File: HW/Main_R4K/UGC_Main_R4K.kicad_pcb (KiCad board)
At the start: 4 copper layers, 125.7 x 76.4 mm, 167 parts, among them J1 SM02B-SURS-TF_LF__SN_, J10 SM02B-SURS-TF_LF__SN_, J13 503480-0640, J2 503480-0640, J4 Conn_01x06_Pin, J5 UJ31-CH-G1-SMT-TR, J6 Trigger, J7 Trigger, J8 Conn_01x02, J9 Conn_01x02, Q1 MMBT3904, Q2 MMBT3904, Q3 BSS138DW, Q4 BSS138DW, Q5 MMBT2222A, Q6 MMBT2222A, SW1 SW_Push, SW10 SW_Push, SW11 SW_Push, SW12 SW_Push, SW13 SW_Push, SW14 SW_TS-1187A, SW15 1TS026A-1000-0550, SW16 1TS026A-1000-0550, SW17 SW_TS-1187A, SW18 SW_TS-1187A, SW19 SW_TS-1187A, SW2 SW_Push, SW3 SW_Push, SW4 SW_Push, SW5 SW_TS-1187A, SW6 GL18_SW, SW7 SW_Push, SW8 SW_Push, SW9 SW_TS-1187A, U1 ESP32-PICO-MINI-02, U10 ST_LSM6, U11 BQ25180, U12 CH340K, U13 PI3USB4000A, U4 TPS630001RCR, U5 ST_LSM6, U6 MCP3002, U7 MCP3002, U8 RP2040, U9 GD25Q80EEIGR, X1 ModConnect, X2 ModConnect, X3 ModConnect, X4 ModConnect, X5 ModConnect, X6 ModConnect, Y1 ABM8-272-T3

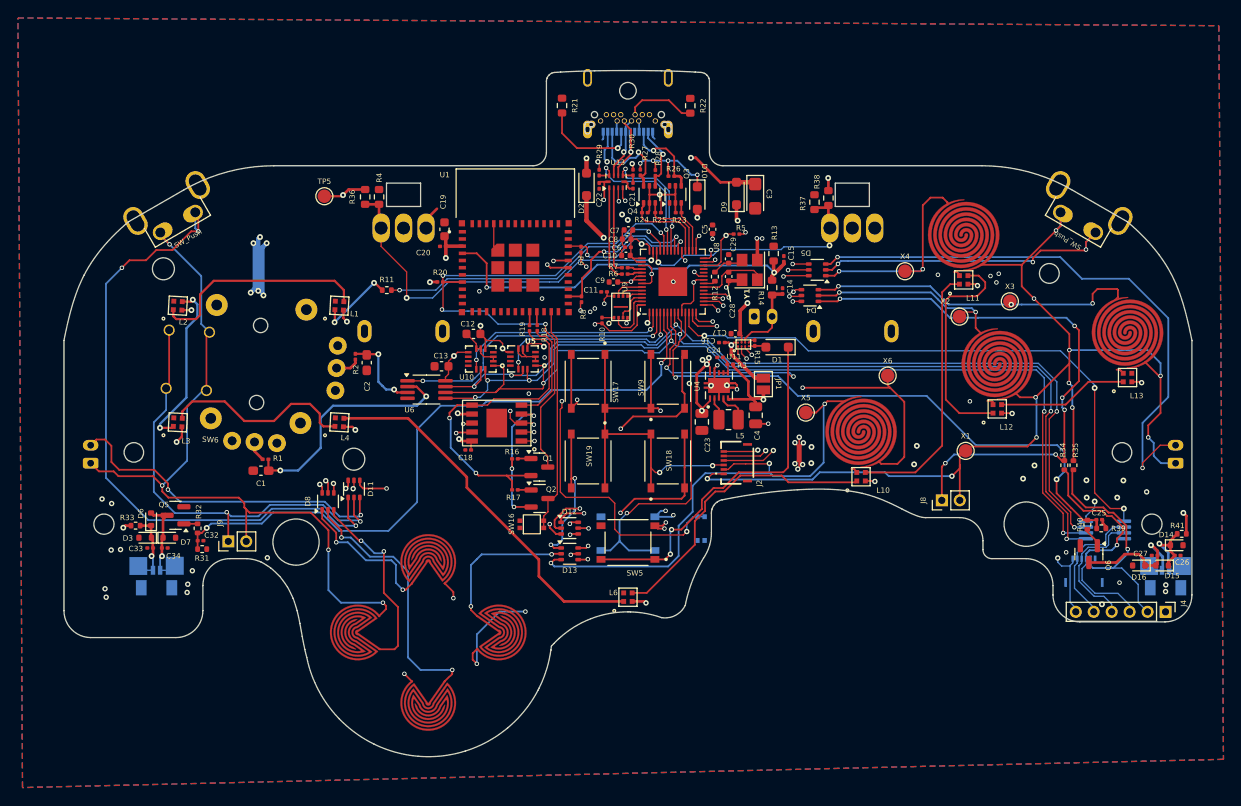
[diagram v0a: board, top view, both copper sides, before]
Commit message: Update PCBs
- Fix BOMs so they reference real part numbers
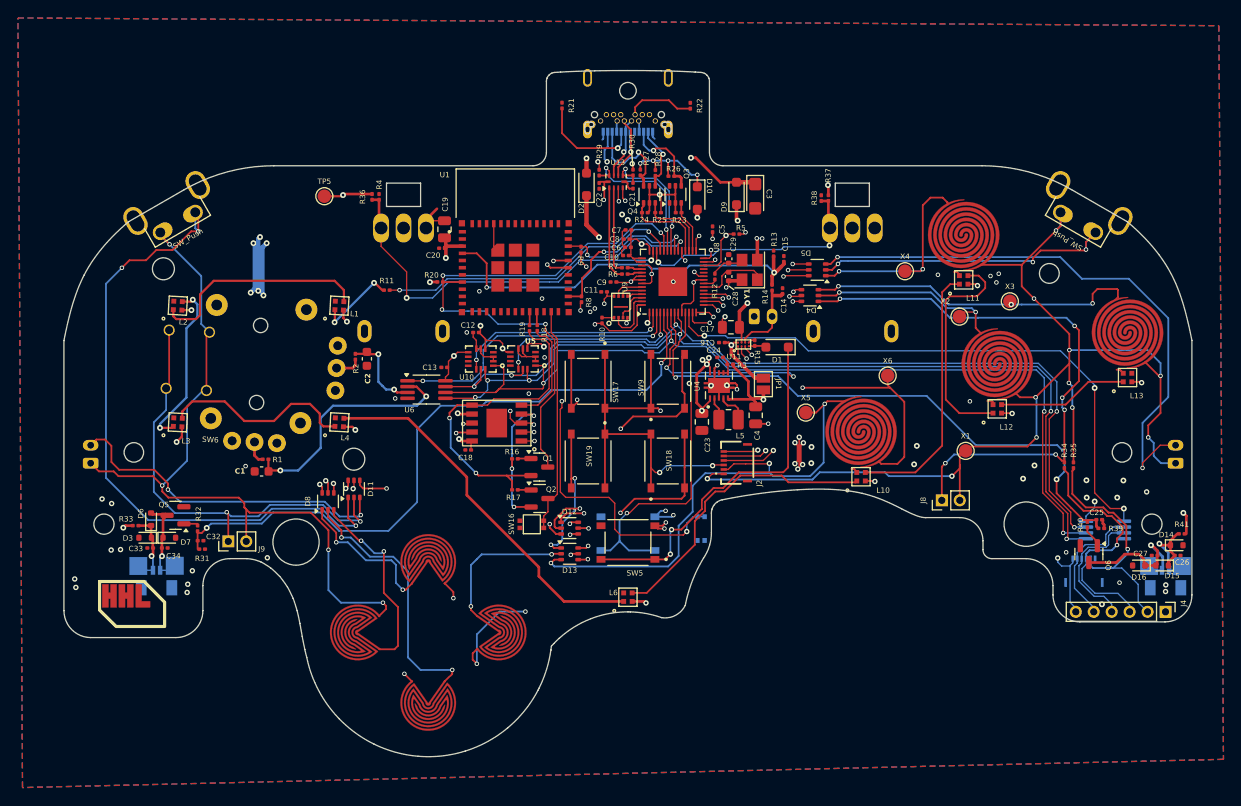
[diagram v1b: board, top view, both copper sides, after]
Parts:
- added REF**: HHL_Logo, hhl:HHL_Logo, F.Cu at (162.6, 143.8)
- C1, C2: value .047u -> 47nF; footprint Capacitor_SMD:C_0603_1608Metric_Pad1.08x0.95mm_HandSolder -> Capacitor_SMD:C_0603_1608Metric
- C10, C5, C7, C9: value 100n -> 100nF; footprint Capacitor_SMD:C_0402_1005Metric -> Capacitor_SMD:C_0201_0603Metric
- C11, C15, C18, C20, C22, C24, C6: value 100n -> 100nF
- C12, C13: footprint Capacitor_SMD:C_0603_1608Metric -> Capacitor_SMD:C_0201_0603Metric
- C14, C16, C21, C26, C27, C33, C34: value 1u -> 1uF
- C17: footprint Capacitor_SMD:C_0402_1005Metric -> Capacitor_SMD:C_0805_2012Metric
- C19: value 10uF/10V (20%) -> 10uF; footprint Capacitor_SMD:C_0603_1608Metric -> Capacitor_SMD:C_0805_2012Metric
- C28, C29: value 15p -> 15pF
- C3: value 47uF 6.3v -> 47uF
- C8: value 1u -> 1uF; footprint Capacitor_SMD:C_0402_1005Metric -> Capacitor_SMD:C_0201_0603Metric
- R11: value 330 -> 330R; footprint Resistor_SMD:R_0402_1005Metric -> Resistor_SMD:R_0201_0603Metric
- R12, R31, R32, R33, R34, R35, R39, R40, R41: footprint Resistor_SMD:R_0402_1005Metric -> Resistor_SMD:R_0201_0603Metric
- R13, R14, R36, R37, R38, R4: footprint Resistor_SMD:R_0603_1608Metric -> Resistor_SMD:R_0201_0603Metric
- R18, R19: value 0 -> 0R
- R21, R22: value 5.1kohm -> 5.1k; footprint Resistor_SMD:R_0603_1608Metric -> Resistor_SMD:R_0201_0603Metric
- R3: value 100 -> 100R
- R6, R7: value 27 -> 27R
- moved R37 0.88 mm to (240.0, 98.1)
- moved C17 0.87 mm to (230.0, 112.5)
- moved R36 0.77 mm to (190.0, 98.0)
- moved C2 0.42 mm to (189.4, 116.0)
- moved C12 0.33 mm to (201.6, 113.1)
- moved C13 0.32 mm to (198.0, 117.0)
- moved C20 0.23 mm to (197.8, 103.7)
- moved C1 0.11 mm to (177.7, 128.6)
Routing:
- net GND: track 56.4 -> 59.9 mm, vias 57 -> 61
- net BAT_LVL: track 44.6 -> 45.6 mm
- net +3V3: track 140.3 -> 141.0 mm
- net H: track 167.0 -> 166.4 mm
- net CC1: track 11.1 -> 11.6 mm
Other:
- board text added: "GCU R4K Designed by Mitch 10.25.2024"
- board text removed: "GCU R4K Designed by Mitch 10.24.2024"
